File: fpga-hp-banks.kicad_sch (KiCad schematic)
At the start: 9 parts, among them U34 XCAU25P-2FFVB676I

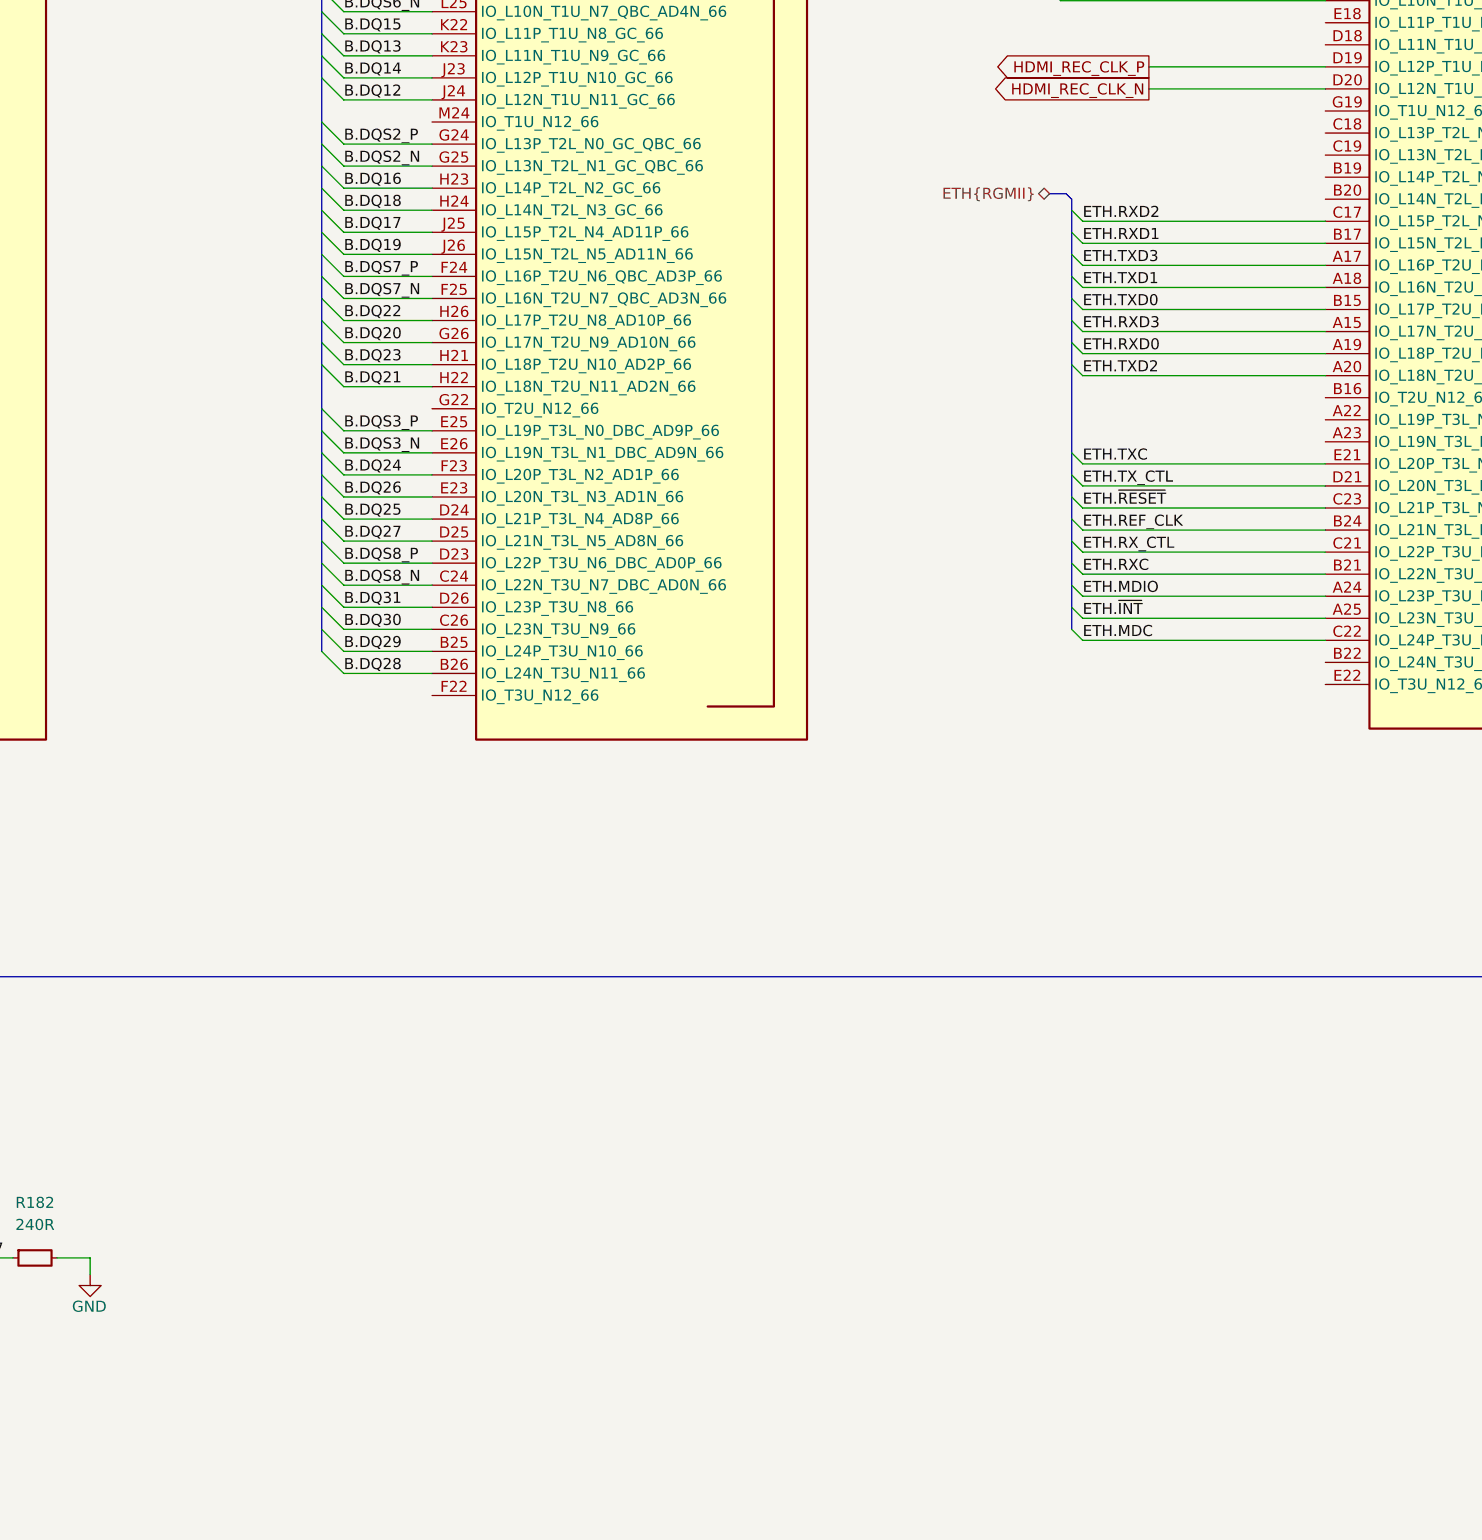
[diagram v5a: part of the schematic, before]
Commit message: [#66312] Added 100MHz LVDS clock source
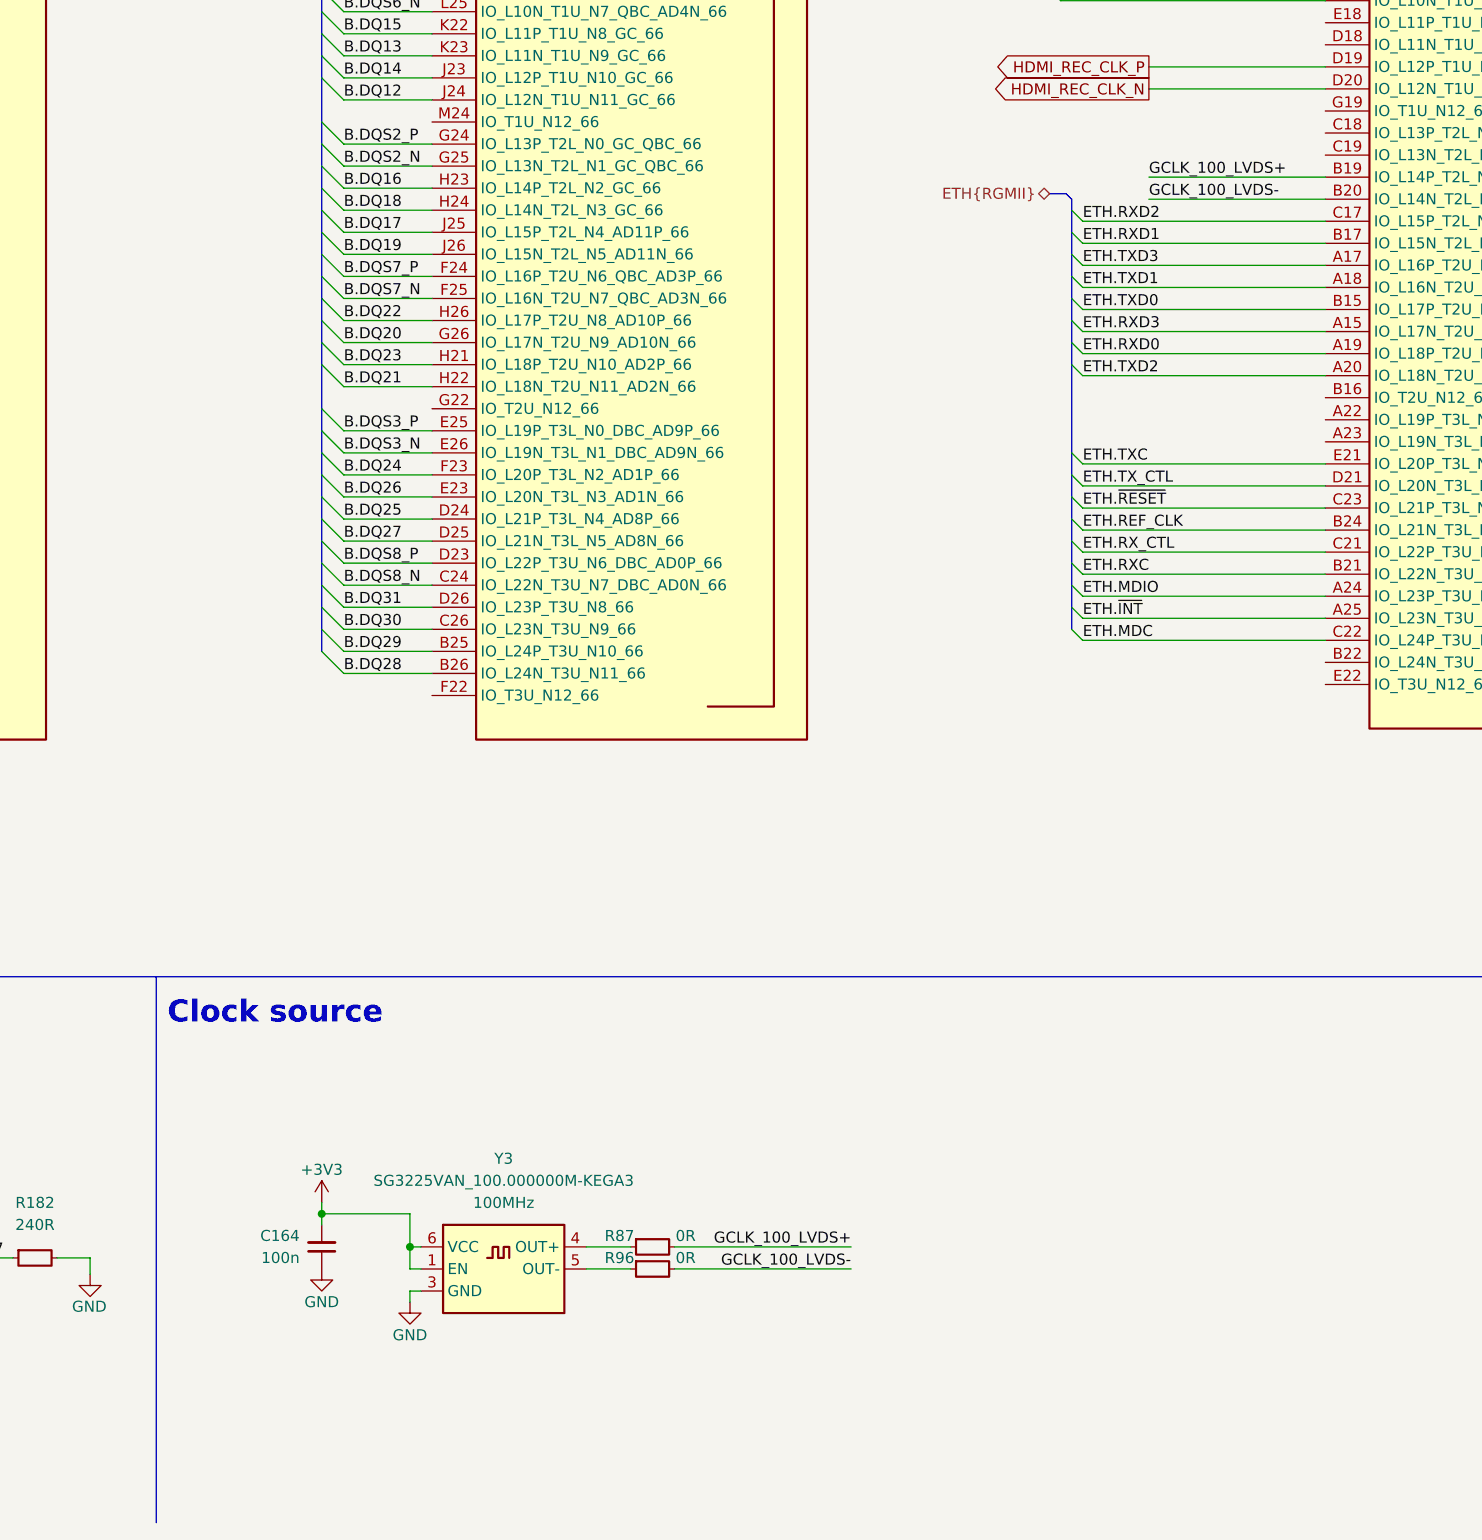
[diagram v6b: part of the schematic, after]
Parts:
- added C164: C_100n_0402, antmicro-footprints:C_0402_1005Metric, symbol antmicroCapacitors0402:C_100n_0402
- added R87, R96: R_0R_0402, antmicro-footprints:R_0402_1005Metric, symbol antmicroResistors0402:R_0R_0402
- added Y3: Oscillator_100MHz_SG3225VAN, antmicro-footprints:Oscillator_SMD_Epson_SG3225EEN_3.2x2.5x1.2mm, symbol antmicroOscillators:Oscillator_100MHz_SG3225VAN
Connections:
- net GND: now also C164.1, Y3.3 (GND)
- net GCLK_100_LVDS+: now reaches U34.B19 (IO_L14P_T2L_N2_GC_67)
- net GCLK_100_LVDS+: now also R87.2
- net GCLK_100_LVDS-: now reaches U34.B20 (IO_L14N_T2L_N3_GC_67)
- net GCLK_100_LVDS-: now also R96.2
- new net: R96.1, Y3.5 (OUT-)
- new net: R87.1, Y3.4 (OUT+)
- new net +3V3: C164.2, Y3.1 (EN), Y3.6 (VCC)
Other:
- note added: "Clock source"

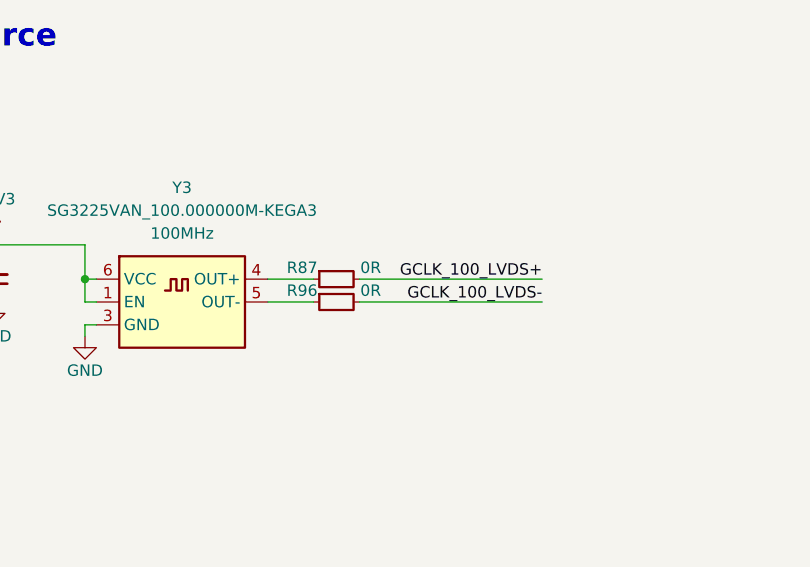
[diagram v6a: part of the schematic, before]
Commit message: [#66312] Remover 0R from GCLK lines
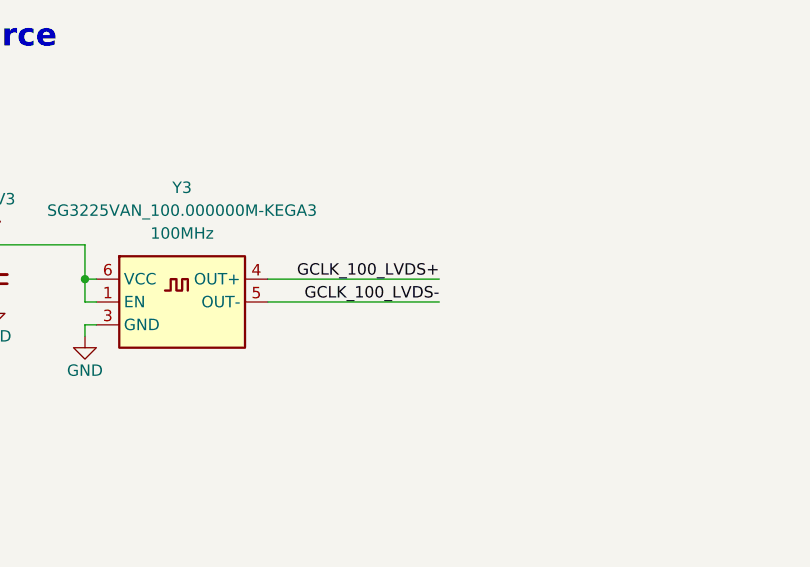
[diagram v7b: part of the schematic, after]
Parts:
- removed R87, R96: R_0R_0402, antmicro-footprints:R_0402_1005Metric, symbol antmicroResistors0402:R_0R_0402
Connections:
- net GCLK_100_LVDS+: now also Y3.4 (OUT+)
- net GCLK_100_LVDS-: now also Y3.5 (OUT-)
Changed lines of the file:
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@@
     (stroke (width 0) (type default))
   )
-  (wire (pts (xy 266.7 252.73) (xy 287.02 252.73))
-    (stroke (width 0) (type default))
-  )
   (wire (pts (xy 228.6 138.43) (xy 238.76 138.43))
     (stroke (width 0) (type default))
@@
     (stroke (width 0) (type default))
   )
-  (wire (pts (xy 256.54 255.27) (xy 261.62 255.27))
-    (stroke (width 0) (type default))
-  )
   (bus (pts (xy 312.42 64.77) (xy 312.42 67.31))
     (stroke (width 0) (type default))
@@
     (stroke (width 0) (type default))
   )
-  (wire (pts (xy 256.54 252.73) (xy 261.62 252.73))
+  (wire (pts (xy 256.54 252.73) (xy 275.59 252.73))
     (stroke (width 0) (type default))
   )
@@
     (stroke (width 0) (type default))
   )
-  (wire (pts (xy 266.7 255.27) (xy 287.02 255.27))
+  (wire (pts (xy 256.54 255.27) (xy 275.59 255.27))
     (stroke (width 0) (type default))
   )
@@
     (effects (font (size 1.27 1.27)) (justify left bottom))
   )
-  (label "GCLK_100_LVDS+" (at 287.02 252.73 180) (fields_autoplaced)
+  (label "GCLK_100_LVDS+" (at 275.59 252.73 180) (fields_autoplaced)
     (effects (font (size 1.27 1.27)) (justify right bottom))
   )
@@
     (effects (font (size 1.27 1.27)) (justify left bottom))
   )
-  (label "GCLK_100_LVDS-" (at 287.02 255.27 180) (fields_autoplaced)
+  (label "GCLK_100_LVDS-" (at 275.59 255.27 180) (fields_autoplaced)
     (effects (font (size 1.27 1.27)) (justify right bottom))
   )
@@
     )
   )
-  (symbol (lib_id "antmicroResistors0402:R_0R_0402") (at 261.62 255.27 0) (unit 1)
-    (in_bom yes) (on_board yes) (dnp no)
-    (property "Reference" "R96" (at 260.35 254 0)
-      (effects (font (size 1.27 1.27) (thickness 0.15)))
-    )
-    (property "Value" "R_0R_0402" (at 281.94 267.97 0)
-      (effects (font (size 1.27 1.27) (thickness 0.15)) (justify left bottom) hide)
-    )
-    (property "Footprint" "antmicro-footprints:R_0402_1005Metric" (at 281.94 270.51 0)
-      (effects (font (size 1.27 1.27) (thickness 0.15)) (justify left bottom) hide)
-    )
-    (property "Datasheet" "https://industrial.panasonic.com/cdbs/www-data/pdf/RDA0000/AOA0000C301.pdf" (at 281.94 273.05 0)
-      (effects (font (size 1.27 1.27) (thickness 0.15)) (justify left bottom) hide)
-    )
-    (property "MPN" "ERJ2GE0R00X" (at 281.94 275.59 0)
-      (effects (font (size 1.27 1.27) (thickness 0.15)) (justify left bottom) hide)
-    )
-    (property "Manufacturer" "Panasonic" (at 281.94 278.13 0)
-      (effects (font (size 1.27 1.27) (thickness 0.15)) (justify left bottom) hide)
-    )
-    (property "License" "Apache-2.0" (at 281.94 280.67 0)
-      (effects (font (size 1.27 1.27) (thickness 0.15)) (justify left bottom) hide)
-    )
-    (property "Author" "Antmicro" (at 281.94 283.21 0)
-      (effects (font (size 1.27 1.27) (thickness 0.15)) (justify left bottom) hide)
-    )
-    (property "Val" "0R" (at 267.97 254 0)
-      (effects (font (size 1.27 1.27) (thickness 0.15)))
-    )
-    (property "Tolerance" "~" (at 281.94 265.43 0)
-      (effects (font (size 1.27 1.27)) (justify left bottom) hide)
-    )
-    (property "Current" "1A" (at 281.94 285.75 0)
-      (effects (font (size 1.27 1.27) (thickness 0.15)) (justify left bottom) hide)
-    )
-    (pin "2")
-    (pin "1")
-    (instances
-      (project "data-center-rdimm-ddr5-tester"
-        (path "/1faa6543-e26a-4449-8bac-ee14b9f19e5f/00000000-0000-0000-0000-000061b4860c"
-          (reference "R96") (unit 1)
-        )
-      )
-    )
-  )
   (symbol (lib_id "antmicroFPGAChips:XCAU25P-2FFVB676I") (at 48.26 50.8 0) (unit 2)
     (in_bom yes) (on_board yes) (dnp no)
@@
         )
       )
-    )
-  )
-  (symbol (lib_id "antmicroResistors0402:R_0R_0402") (at 261.62 252.73 0) (unit 1)
-    (in_bom yes) (on_board yes) (dnp no)
-    (property "Reference" "R87" (at 260.35 251.46 0)
-      (effects (font (size 1.27 1.27) (thickness 0.15)))
-    )
-    (property "Value" "R_0R_0402" (at 281.94 265.43 0)
-      (effects (font (size 1.27 1.27) (thickness 0.15)) (justify left bottom) hide)
-    )
-    (property "Footprint" "antmicro-footprints:R_0402_1005Metric" (at 281.94 267.97 0)
-      (effects (font (size 1.27 1.27) (thickness 0.15)) (justify left bottom) hide)
-    )
-    (property "Datasheet" "https://industrial.panasonic.com/cdbs/www-data/pdf/RDA0000/AOA0000C301.pdf" (at 281.94 270.51 0)
-      (effects (font (size 1.27 1.27) (thickness 0.15)) (justify left bottom) hide)
-    )
-    (property "MPN" "ERJ2GE0R00X" (at 281.94 273.05 0)
-      (effects (font (size 1.27 1.27) (thickness 0.15)) (justify left bottom) hide)
-    )
-    (property "Manufacturer" "Panasonic" (at 281.94 275.59 0)
-      (effects (font (size 1.27 1.27) (thickness 0.15)) (justify left bottom) hide)
-    )
-    (property "License" "Apache-2.0" (at 281.94 278.13 0)
-      (effects (font (size 1.27 1.27) (thickness 0.15)) (justify left bottom) hide)
-    )
-    (property "Author" "Antmicro" (at 281.94 280.67 0)
-      (effects (font (size 1.27 1.27) (thickness 0.15)) (justify left bottom) hide)
-    )
-    (property "Val" "0R" (at 267.97 251.46 0)
-      (effects (font (size 1.27 1.27) (thickness 0.15)))
-    )
-    (property "Tolerance" "~" (at 281.94 262.89 0)
-      (effects (font (size 1.27 1.27)) (justify left bottom) hide)
-    )
-    (property "Current" "1A" (at 281.94 283.21 0)
-      (effects (font (size 1.27 1.27) (thickness 0.15)) (justify left bottom) hide)
-    )
-    (pin "2")
-    (pin "1")
-    (instances
-      (project "data-center-rdimm-ddr5-tester"
-        (path "/1faa6543-e26a-4449-8bac-ee14b9f19e5f/00000000-0000-0000-0000-000061b4860c"
-          (reference "R87") (unit 1)
-        )
-      )

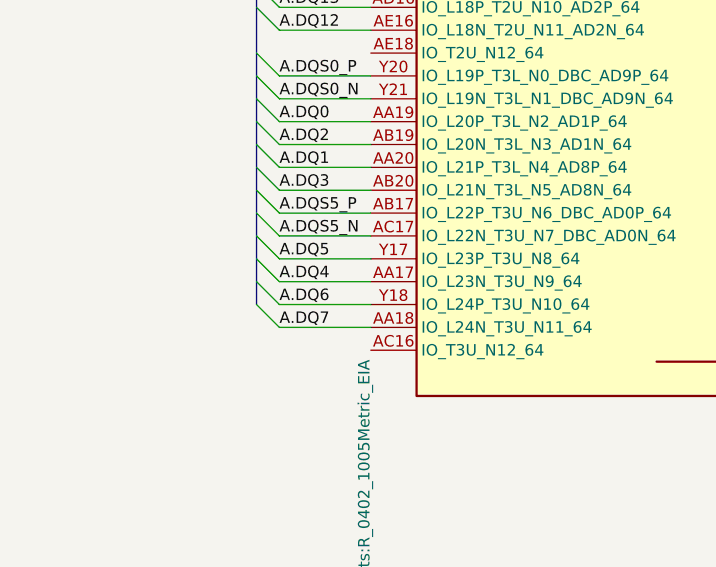
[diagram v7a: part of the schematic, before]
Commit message: [#66727] Fix schematic errors
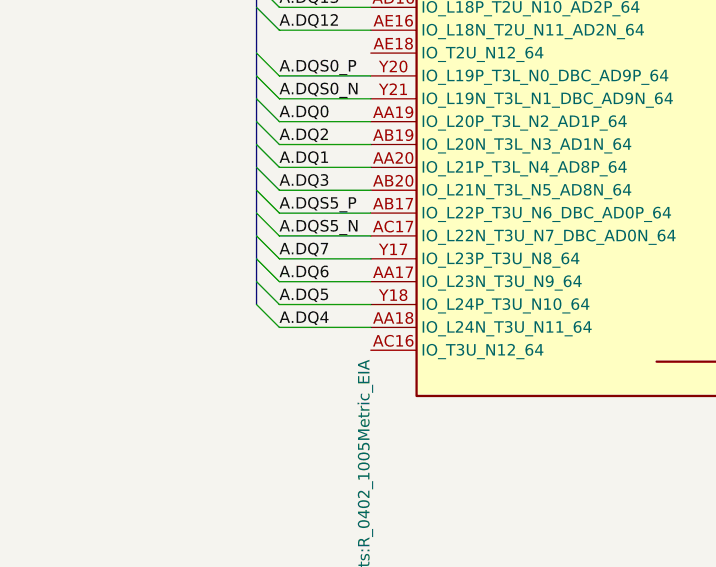
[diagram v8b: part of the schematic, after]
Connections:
- net A.DQ4: now also U34.AA18 (IO_L24N_T3U_N11_64); no longer U34.AA17 (IO_L23N_T3U_N9_64)
- net A.DQ5: now also U34.Y18 (IO_L24P_T3U_N10_64); no longer U34.Y17 (IO_L23P_T3U_N8_64)
- net A.DQ6: now also U34.AA17 (IO_L23N_T3U_N9_64); no longer U34.Y18 (IO_L24P_T3U_N10_64)
- net A.DQ7: now also U34.Y17 (IO_L23P_T3U_N8_64); no longer U34.AA18 (IO_L24N_T3U_N11_64)
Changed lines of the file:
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@@
     (effects (font (size 1.27 1.27)) (justify left bottom))
   )
-  (label "A.DQ5" (at 38.1 177.8 0) (fields_autoplaced)
+  (label "A.DQ5" (at 38.1 182.88 0) (fields_autoplaced)
     (effects (font (size 1.27 1.27)) (justify left bottom))
   )
@@
     (effects (font (size 1.27 1.27)) (justify left bottom))
   )
-  (label "A.DQ6" (at 38.1 182.88 0) (fields_autoplaced)
+  (label "A.DQ6" (at 38.1 180.34 0) (fields_autoplaced)
     (effects (font (size 1.27 1.27)) (justify left bottom))
   )
@@
     (effects (font (size 1.27 1.27)) (justify left bottom))
   )
-  (label "A.DQ4" (at 38.1 180.34 0) (fields_autoplaced)
+  (label "A.DQ4" (at 38.1 185.42 0) (fields_autoplaced)
     (effects (font (size 1.27 1.27)) (justify left bottom))
   )
@@
     (effects (font (size 1.27 1.27)) (justify left bottom))
   )
-  (label "A.DQ7" (at 38.1 185.42 0) (fields_autoplaced)
-    (effects (font (size 1.27 1.27)) (justify left bottom))
-  )
+  (label "A.DQ7" (at 38.1 177.8 0) (fields_autoplaced)
+    (effects (font (size 1.27 1.27)) (justify left bottom))
+  )
